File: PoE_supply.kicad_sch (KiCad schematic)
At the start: 23 parts, among them J1 Bus_RJ45_5-2337992-8, Q1 PJE138K, U1 TPS2372-3RGWR, U4 IEA48003A280V-001-R

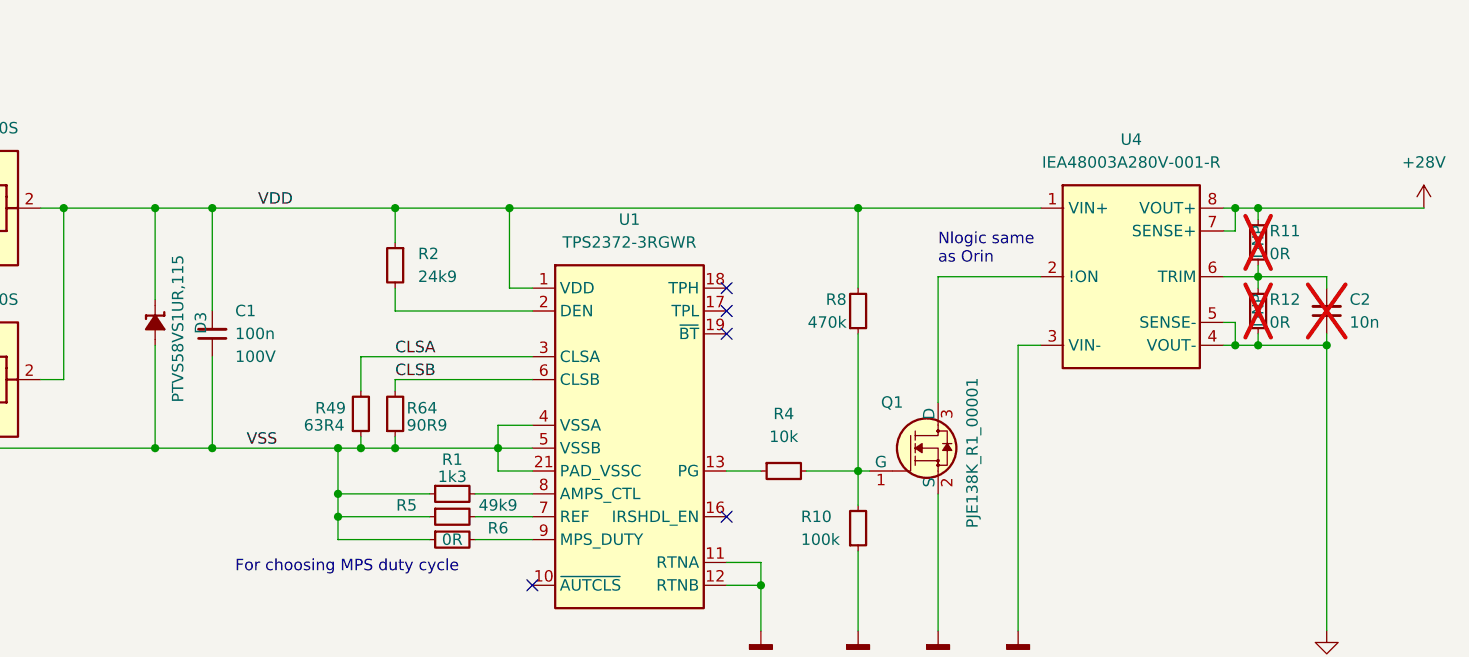
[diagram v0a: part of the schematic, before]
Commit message: [#62835] Tacle ERC problems, add PWR flags
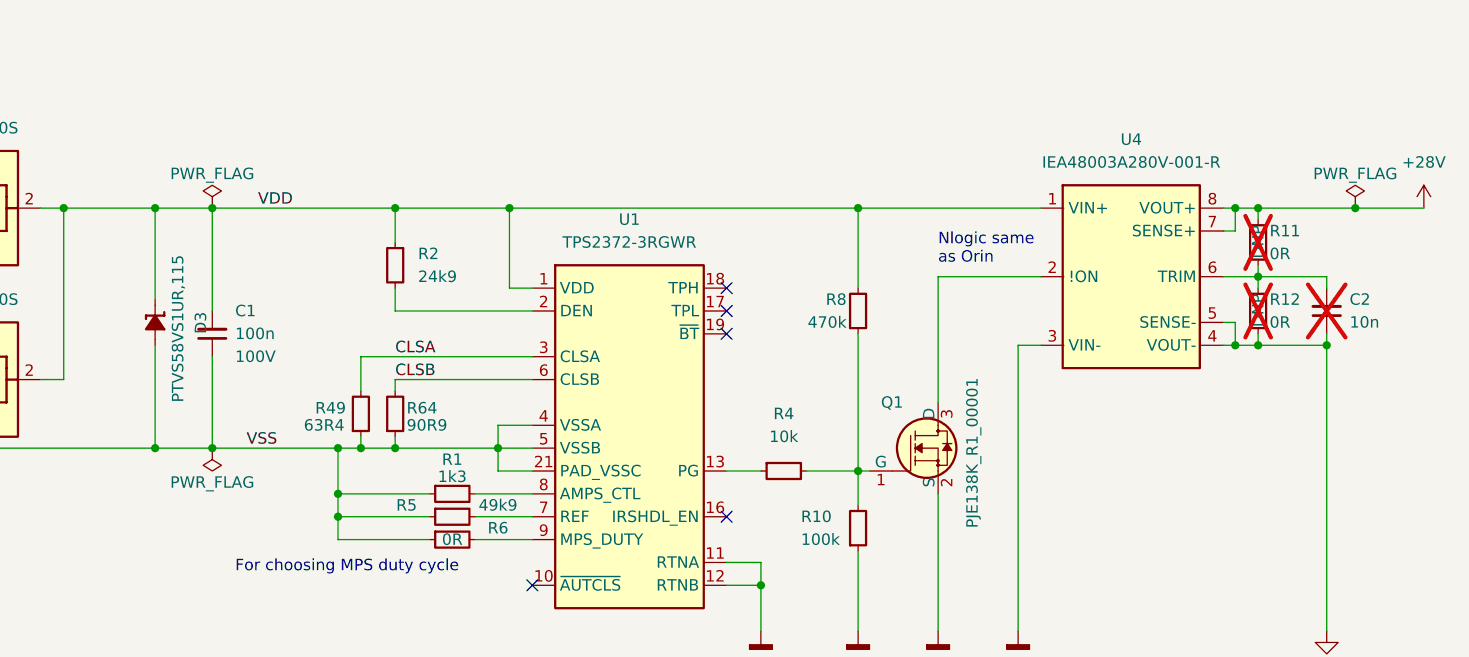
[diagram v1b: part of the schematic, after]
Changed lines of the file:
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@@
   (junction (at 189.865 134.62) (diameter 0) (color 0 0 0 0)
+  )
+  (junction (at 323.215 107.95) (diameter 0) (color 0 0 0 0)
   )
   (junction (at 123.19 127) (diameter 0) (color 0 0 0 0)
@@
     (stroke (width 0) (type default))
   )
-  (wire (pts (xy 312.42 107.95) (xy 330.835 107.95))
+  (wire (pts (xy 312.42 107.95) (xy 323.215 107.95))
     (stroke (width 0) (type default))
   )
   (wire (pts (xy 179.705 107.95) (xy 189.865 107.95))
+    (stroke (width 0) (type default))
+  )
+  (wire (pts (xy 323.215 107.95) (xy 330.835 107.95))
     (stroke (width 0) (type default))
   )
@@
         (path "/cf0d4429-3f03-449f-96a7-26d69371a46d/a2b30c81-e263-4971-9235-45a28ceb7112"
           (reference "R1") (unit 1)
+        )
+      )
+    )
+  )
+  (symbol (lib_id "antmicropower:PWR_FLAG") (at 196.215 107.95 0) (unit 1)
+    (in_bom yes) (on_board yes) (dnp no)
+    (property "Reference" "#FLG012" (at 196.215 106.045 0)
+      (effects (font (size 1.27 1.27)) hide)
+    )
+    (property "Value" "PWR_FLAG" (at 196.215 104.14 0)
+      (effects (font (size 1.27 1.27)))
+    )
+    (property "Footprint" "" (at 196.215 107.95 0)
+      (effects (font (size 1.27 1.27)) hide)
+    )
+    (property "Datasheet" "" (at 196.215 107.95 0)
+      (effects (font (size 1.27 1.27)) hide)
+    )
+    (pin "1")
+    (instances
+      (project "antmicro-poe-to-usbc-pd-adapter"
+        (path "/cf0d4429-3f03-449f-96a7-26d69371a46d/a2b30c81-e263-4971-9235-45a28ceb7112"
+          (reference "#FLG012") (unit 1)
         )
       )
@@
     )
   )
+  (symbol (lib_id "antmicropower:PWR_FLAG") (at 323.215 107.95 0) (unit 1)
+    (in_bom yes) (on_board yes) (dnp no)
+    (property "Reference" "#FLG07" (at 323.215 106.045 0)
+      (effects (font (size 1.27 1.27)) hide)
+    )
+    (property "Value" "PWR_FLAG" (at 323.215 104.14 0)
+      (effects (font (size 1.27 1.27)))
+    )
+    (property "Footprint" "" (at 323.215 107.95 0)
+      (effects (font (size 1.27 1.27)) hide)
+    )
+    (property "Datasheet" "" (at 323.215 107.95 0)
+      (effects (font (size 1.27 1.27)) hide)
+    )
+    (pin "1")
+    (instances
+      (project "antmicro-poe-to-usbc-pd-adapter"
+        (path "/cf0d4429-3f03-449f-96a7-26d69371a46d/a2b30c81-e263-4971-9235-45a28ceb7112"
+          (reference "#FLG07") (unit 1)
+        )
+      )
+    )
+  )
   (symbol (lib_id "antmicroCapacitorsmisc:C_100n_100V_0805") (at 196.215 124.46 90) (unit 1)
     (in_bom yes) (on_board yes) (dnp no) (fields_autoplaced)
@@
         )
       )
+    )
+  )
+  (symbol (lib_id "antmicropower:PWR_FLAG") (at 196.215 134.62 180) (unit 1)
+    (in_bom yes) (on_board yes) (dnp no)
+    (property "Reference" "#FLG08" (at 196.215 136.525 0)
+      (effects (font (size 1.27 1.27)) hide)
+    )
+    (property "Value" "PWR_FLAG" (at 196.215 138.43 0)
+      (effects (font (size 1.27 1.27)))
+    )
+    (property "Footprint" "" (at 196.215 134.62 0)
+      (effects (font (size 1.27 1.27)) hide)
+    )
+    (property "Datasheet" "" (at 196.215 134.62 0)
+      (effects (font (size 1.27 1.27)) hide)
+    )
+    (pin "1")
+    (instances
+      (project "antmicro-poe-to-usbc-pd-adapter"
+        (path "/cf0d4429-3f03-449f-96a7-26d69371a46d/a2b30c81-e263-4971-9235-45a28ceb7112"
+          (reference "#FLG08") (unit 1)
+        )
+      )

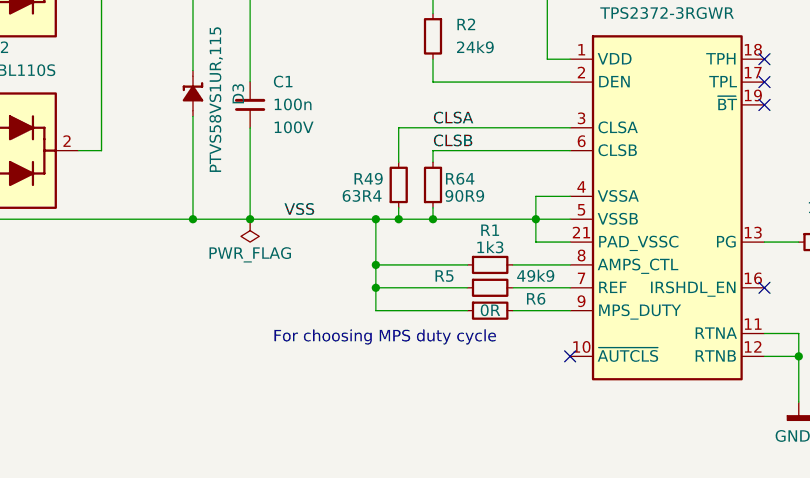
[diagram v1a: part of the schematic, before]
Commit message: [#62835] Add vias, second GND plane, GNDD plane, lower INA IC, minor changes
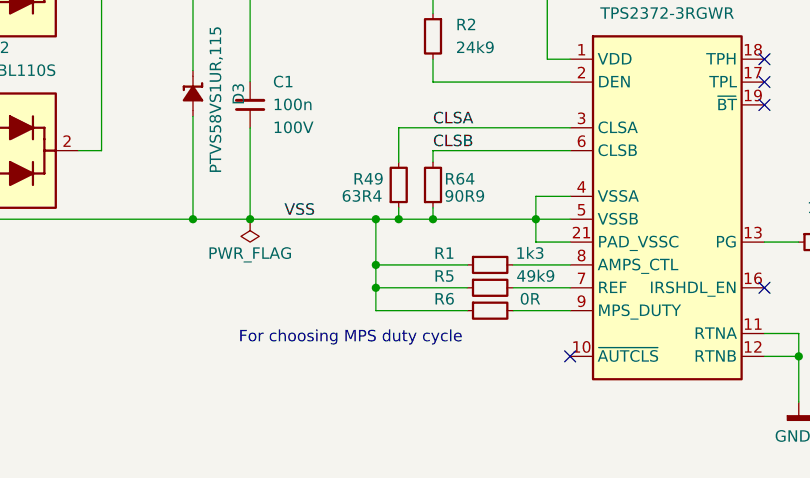
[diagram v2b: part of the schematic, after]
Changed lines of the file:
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@@
     (effects (font (size 1.27 1.27)) (justify left bottom))
   )
-  (text "For choosing MPS duty cycle" (at 198.755 148.59 0)
+  (text "For choosing MPS duty cycle" (at 194.945 148.59 0)
     (effects (font (size 1.27 1.27)) (justify left bottom))
   )
@@
   (hierarchical_label "{ETH}" (shape output) (at 26.67 22.86 180) (fields_autoplaced)
     (effects (font (size 1.27 1.27)) (justify right))
+  )
+  (netclass_flag "" (length 2.54) (shape round) (at 265.43 137.16 0)
+    (effects (font (size 1.27 1.27)) (justify left bottom))
+    (property "Netclass" "PoE" (at 263.525 133.35 0)
+      (effects (font (size 1.27 1.27) italic) (justify left))
+    )
+  )
+  (netclass_flag "" (length 2.54) (shape round) (at 226.06 134.62 0)
+    (effects (font (size 1.27 1.27)) (justify left bottom))
+    (property "Netclass" "PoE" (at 224.155 130.81 0)
+      (effects (font (size 1.27 1.27) italic) (justify left))
+    )
+  )
+  (netclass_flag "" (length 2.54) (shape round) (at 226.06 144.78 180)
+    (effects (font (size 1.27 1.27)) (justify right bottom))
+    (property "Netclass" "PoE" (at 227.965 148.59 0)
+      (effects (font (size 1.27 1.27) italic) (justify right))
+    )
+  )
+  (netclass_flag "" (length 2.54) (shape round) (at 280.67 115.57 180)
+    (effects (font (size 1.27 1.27)) (justify right bottom))
+    (property "Netclass" "PoE" (at 282.575 119.38 0)
+      (effects (font (size 1.27 1.27) italic) (justify right))
+    )
+  )
+  (netclass_flag "" (length 2.54) (shape round) (at 250.825 127 270)
+    (effects (font (size 1.27 1.27)) (justify right bottom))
+    (property "Netclass" "PoE" (at 255.27 125.095 0)
+      (effects (font (size 1.27 1.27) italic) (justify right))
+    )
+  )
+  (netclass_flag "" (length 2.54) (shape round) (at 226.695 119.38 0)
+    (effects (font (size 1.27 1.27)) (justify left bottom))
+    (property "Netclass" "PoE" (at 224.79 115.57 0)
+      (effects (font (size 1.27 1.27) italic) (justify left))
+    )
+  )
+  (netclass_flag "" (length 2.54) (shape round) (at 250.825 129.54 270)
+    (effects (font (size 1.27 1.27)) (justify right bottom))
+    (property "Netclass" "PoE" (at 255.27 128.27 0)
+      (effects (font (size 1.27 1.27) italic) (justify right))
+    )
+  )
+  (netclass_flag "" (length 2.54) (shape round) (at 255.27 137.16 0)
+    (effects (font (size 1.27 1.27)) (justify left bottom))
+    (property "Netclass" "PoE" (at 253.365 133.35 0)
+      (effects (font (size 1.27 1.27) italic) (justify left))
+    )
+  )
+  (netclass_flag "" (length 2.54) (shape round) (at 250.825 132.08 270)
+    (effects (font (size 1.27 1.27)) (justify right bottom))
+    (property "Netclass" "PoE" (at 255.27 130.81 0)
+      (effects (font (size 1.27 1.27) italic) (justify right))
+    )
+  )
+  (netclass_flag "" (length 2.54) (shape round) (at 257.175 147.32 0)
+    (effects (font (size 1.27 1.27)) (justify left bottom))
+    (property "Netclass" "PoE" (at 255.27 143.51 0)
+      (effects (font (size 1.27 1.27) italic) (justify left))
+    )
+  )
+  (netclass_flag "" (length 2.54) (shape round) (at 230.505 142.24 180)
+    (effects (font (size 1.27 1.27)) (justify right bottom))
+    (property "Netclass" "PoE" (at 232.41 146.05 0)
+      (effects (font (size 1.27 1.27) italic) (justify right))
+    )
+  )
+  (netclass_flag "" (length 2.54) (shape round) (at 231.775 149.86 180)
+    (effects (font (size 1.27 1.27)) (justify right bottom))
+    (property "Netclass" "PoE" (at 229.87 153.67 0)
+      (effects (font (size 1.27 1.27) italic) (justify left))
+    )
+  )
+  (netclass_flag "" (length 2.54) (shape round) (at 225.425 139.7 0)
+    (effects (font (size 1.27 1.27)) (justify left bottom))
+    (property "Netclass" "PoE" (at 223.52 135.89 0)
+      (effects (font (size 1.27 1.27) italic) (justify left))
+    )
   )
   (netclass_flag "" (length 2.54) (shape round) (at 123.19 125.73 0) (fields_autoplaced)
@@
   (symbol (lib_id "antmicroResistors0603:R_1k3_0603") (at 220.345 139.7 0) (unit 1)
     (in_bom yes) (on_board yes) (dnp no)
-    (property "Reference" "R1" (at 222.885 135.89 0)
+    (property "Reference" "R1" (at 217.805 138.43 0)
       (effects (font (size 1.27 1.27) (thickness 0.15)))
     )
@@
       (effects (font (size 1.27 1.27) (thickness 0.15)) (justify left bottom) hide)
     )
-    (property "Val" "1k3" (at 222.885 137.795 0)
+    (property "Val" "1k3" (at 227.33 138.43 0)
       (effects (font (size 1.27 1.27) (thickness 0.15)))
     )
@@
   (symbol (lib_id "antmicroResistors0402:R_0R_0402") (at 220.345 144.78 0) (unit 1)
     (in_bom yes) (on_board yes) (dnp no)
-    (property "Reference" "R6" (at 227.965 143.51 0)
+    (property "Reference" "R6" (at 217.805 143.51 0)
       (effects (font (size 1.27 1.27) (thickness 0.15)))
     )
@@
       (effects (font (size 1.27 1.27) (thickness 0.15)) (justify left bottom) hide)
     )
-    (property "Val" "0R" (at 222.885 144.78 0)
-      (effects (font (size 1.27 1.27) (thickness 0.15)))
-    )
+    (property "Val" "0R" (at 227.33 143.51 0)
+      (effects (font (size 1.27 1.27) (thickness 0.15)))
+    )

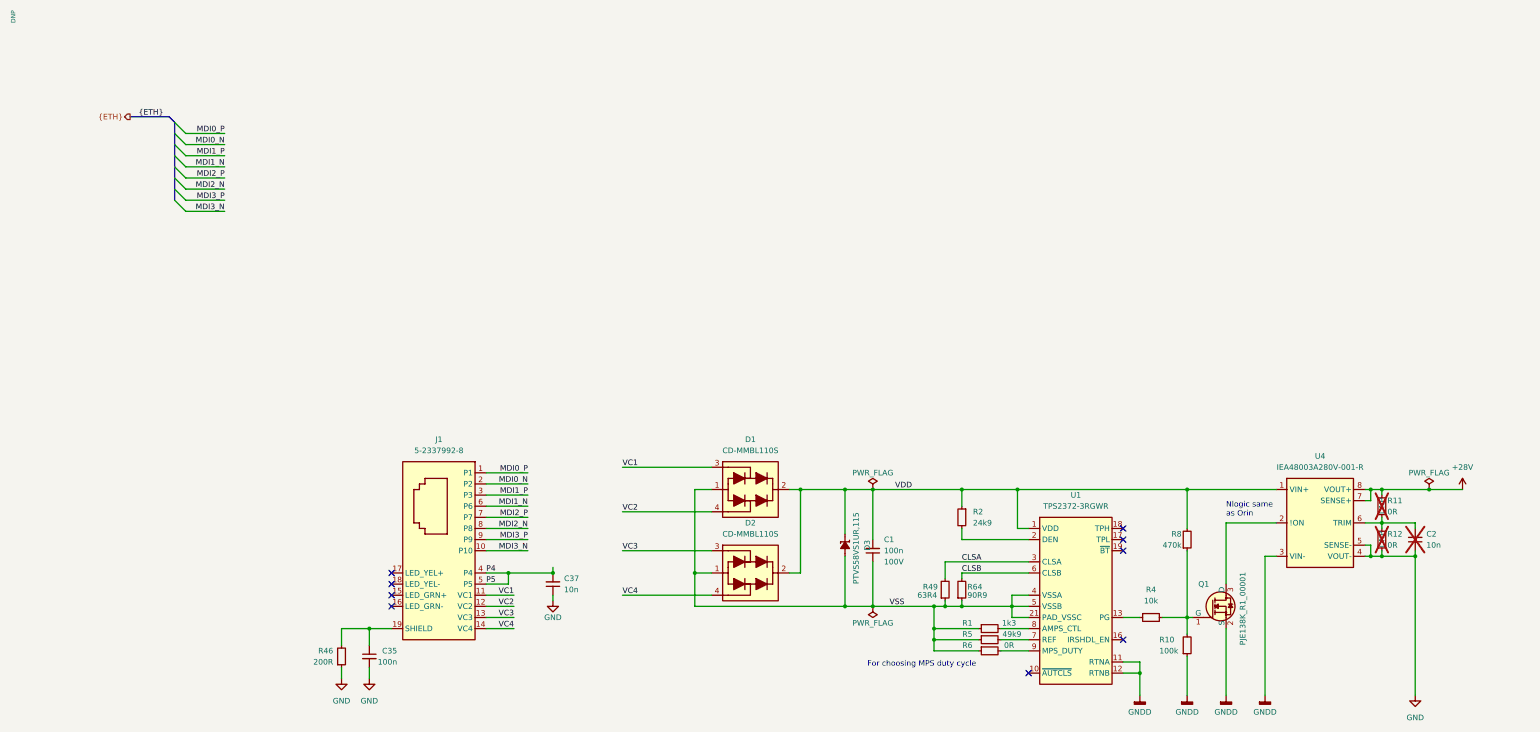
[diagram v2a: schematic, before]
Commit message: [#62835] PoE to USB-C PD Review Rev.1.0.0 correct points 1,3,4,6,7,11
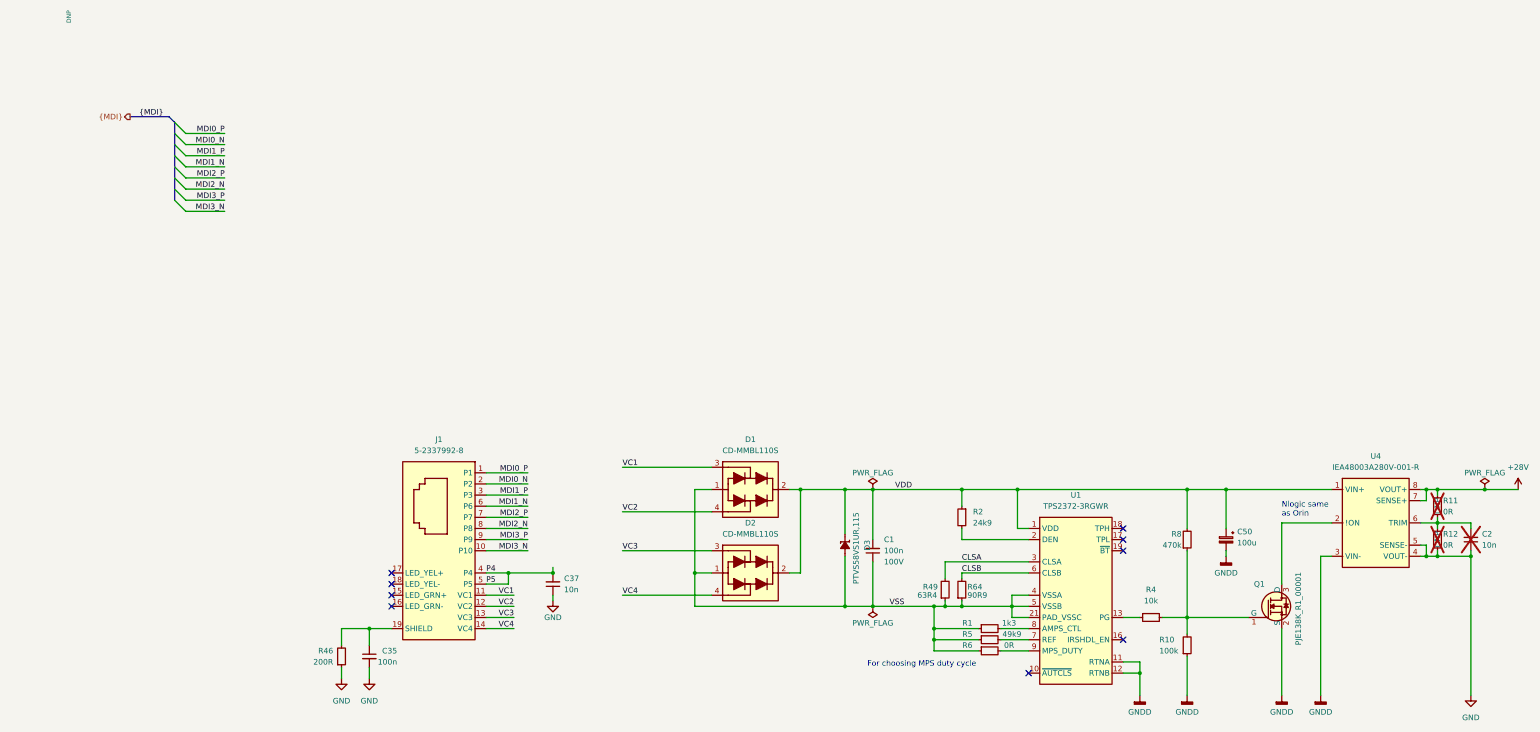
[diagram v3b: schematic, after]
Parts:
- added C50: C_Pol_100u_100V_Vishay-150-CRZ-1213-D12.5mm-H13mm, antmicro-footprints:C_Pol_Vishay-1213-D12.5mm-H13mm, symbol antmicroCapacitorspol:C_Pol_100u_100V_Vishay-150-CRZ-1213-D12.5mm-H13mm
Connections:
- net GNDD: now also C50.2
- net VDD: now also C50.1
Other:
- company: (none) -> Antmicro ltd.
- title: (none) -> PoE to USBC PD adapter
- moved on the sheet: C2, Q1, R11, R12, U4
